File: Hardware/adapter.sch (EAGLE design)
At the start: 6 parts

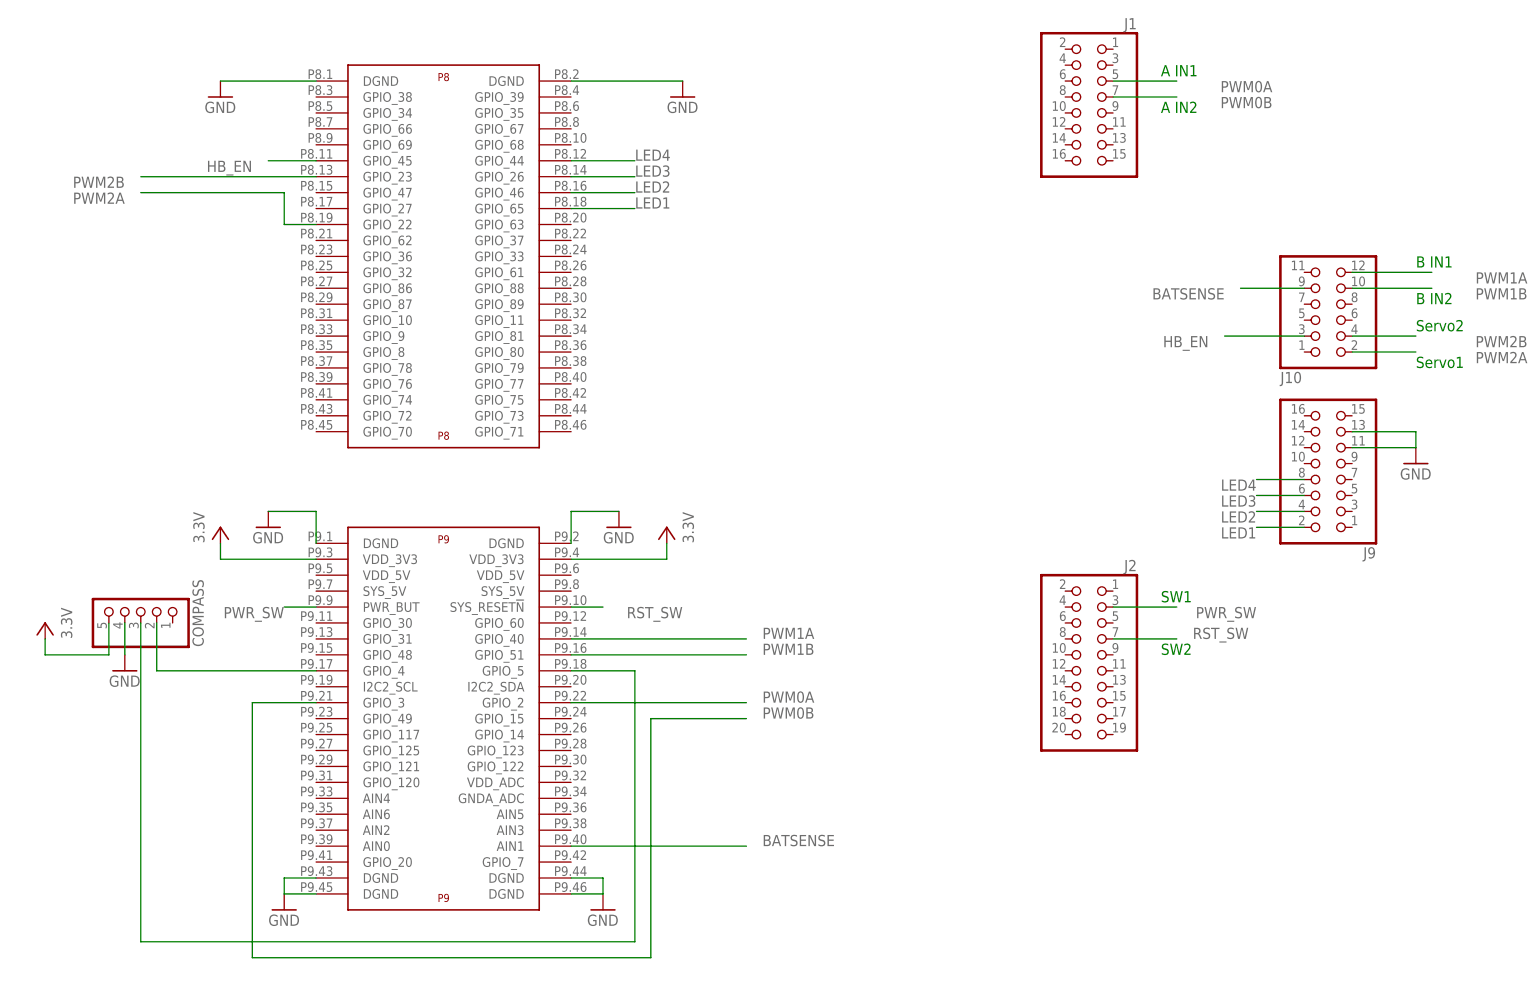
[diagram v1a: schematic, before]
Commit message: Added 5V regulator. Fixed J9 flip issue.
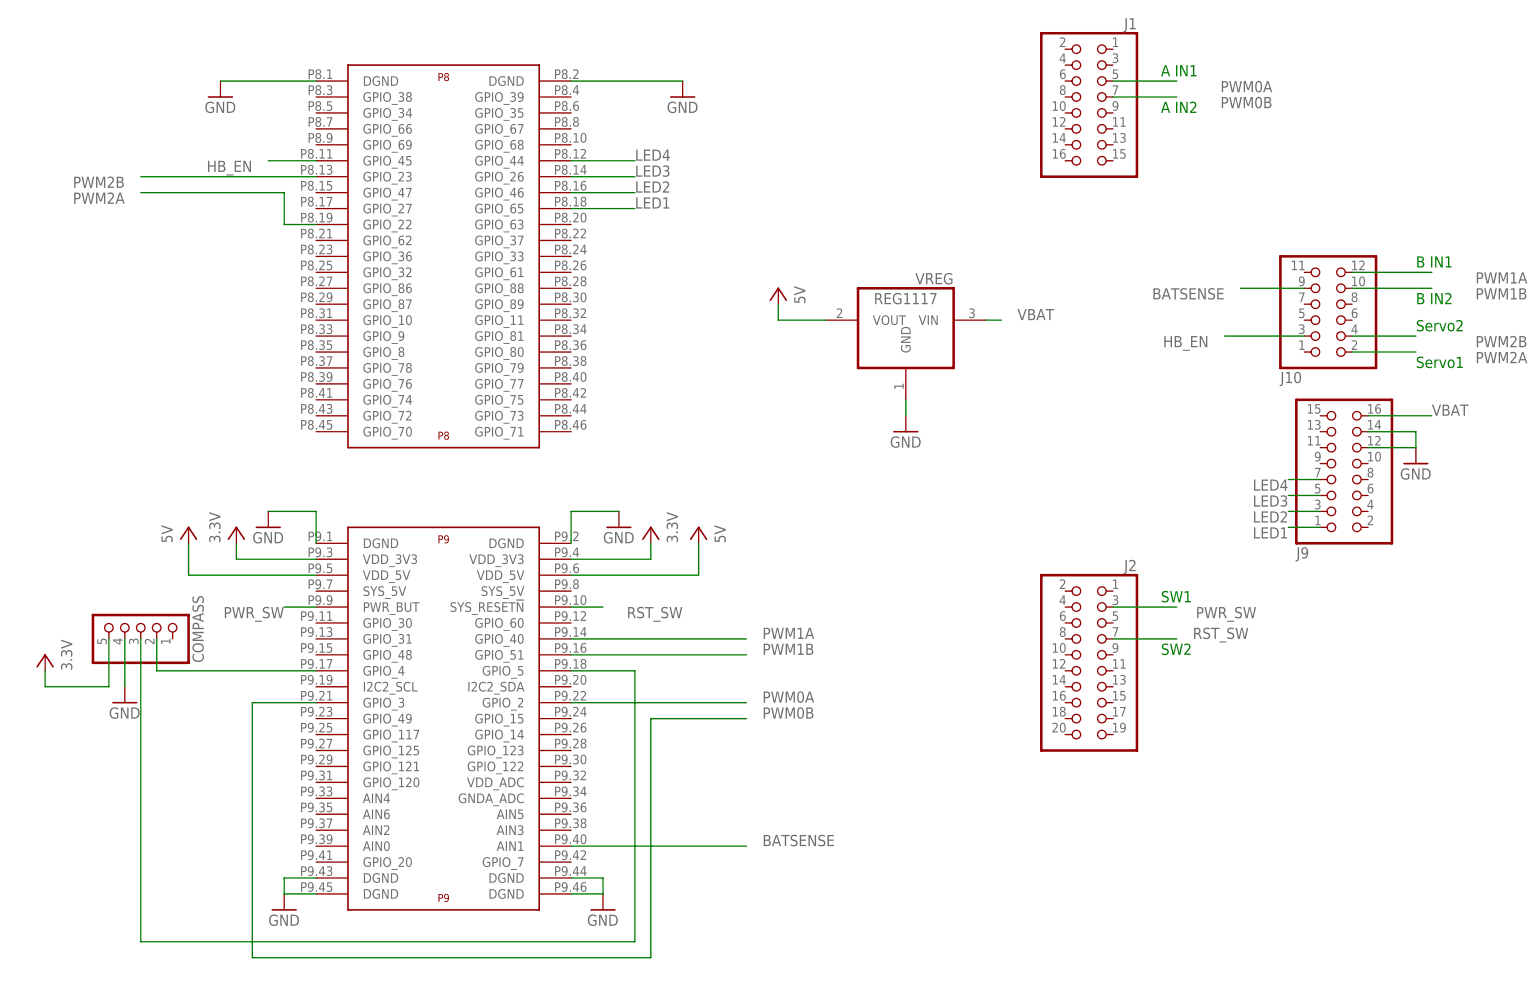
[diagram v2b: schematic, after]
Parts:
- added VREG: REG1117, burr-brown:REG1117
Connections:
- new net 5V: U$1P9.VDD_5V@1, U$1P9.VDD_5V@2, VREG.VOUT
- new net VBAT: J9.16, VREG.VIN
- net GND: now also J9.12, J9.14, VREG.GND; no longer J9.11, J9.13
- net LED1: now also J9.1; no longer J9.2
- net LED2: now also J9.3; no longer J9.4
- net LED3: now also J9.5; no longer J9.6
- net LED4: now also J9.7; no longer J9.8
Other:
- moved on the sheet: COMPASS, J9
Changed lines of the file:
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@@
 <part name="J1" library="pinhead" deviceset="PINHD-2X8" device=""/>
 <part name="J9" library="pinhead" deviceset="PINHD-2X8" device=""/>
+<part name="VREG" library="burr-brown" deviceset="REG1117" device=""/>
+<part name="GND9" library="supply1" deviceset="GND" device=""/>
+<part name="5V" library="supply1" deviceset="VCC" device="" value="5V"/>
+<part name="5V1" library="supply1" deviceset="VCC" device="" value="5V"/>
+<part name="5V2" library="supply1" deviceset="VCC" device="" value="5V"/>
 </parts>
 <sheets>
@@
 <instance part="GND6" gate="1" x="43.18" y="-10.16"/>
 <instance part="GND7" gate="1" x="172.72" y="60.96"/>
-<instance part="COMPASS" gate="A" x="-30.48" y="38.1" rot="MR90"/>
-<instance part="GND8" gate="1" x="-33.02" y="27.94"/>
-<instance part="P+1" gate="VCC" x="-45.72" y="35.56" rot="MR0"/>
-<instance part="P+2" gate="VCC" x="-17.78" y="50.8"/>
-<instance part="P+3" gate="VCC" x="53.34" y="50.8" rot="MR0"/>
+<instance part="COMPASS" gate="A" x="-30.48" y="35.56" rot="MR90"/>
+<instance part="GND8" gate="1" x="-33.02" y="22.86"/>
+<instance part="P+1" gate="VCC" x="-45.72" y="30.48" rot="MR0"/>
+<instance part="P+2" gate="VCC" x="-15.24" y="50.8"/>
+<instance part="P+3" gate="VCC" x="50.8" y="50.8" rot="MR0"/>
 <instance part="J1" gate="A" x="121.92" y="119.38" rot="MR0"/>
-<instance part="J9" gate="A" x="160.02" y="58.42" rot="R180"/>
+<instance part="J9" gate="A" x="160.02" y="58.42" rot="MR180"/>
+<instance part="VREG" gate="G$1" x="91.44" y="83.82" rot="MR0"/>
+<instance part="GND9" gate="1" x="91.44" y="66.04"/>
+<instance part="5V" gate="VCC" x="71.12" y="88.9" rot="MR0"/>
+<instance part="5V1" gate="VCC" x="58.42" y="50.8" rot="MR0"/>
+<instance part="5V2" gate="VCC" x="-22.86" y="50.8"/>
 </instances>
 <busses>
@@
 <segment>
 <pinref part="COMPASS" gate="A" pin="4"/>
-<wire x1="-33.02" y1="35.56" x2="-33.02" y2="30.48" width="0.1524" layer="91"/>
+<wire x1="-33.02" y1="33.02" x2="-33.02" y2="25.4" width="0.1524" layer="91"/>
 <pinref part="GND8" gate="1" pin="GND"/>
 </segment>
@@
 </segment>
 <segment>
+<pinref part="GND9" gate="1" pin="GND"/>
+<pinref part="VREG" gate="G$1" pin="GND"/>
+<wire x1="91.44" y1="68.58" x2="91.44" y2="71.12" width="0.1524" layer="91"/>
+</segment>
+<segment>
+<pinref part="J9" gate="A" pin="14"/>
 <pinref part="GND7" gate="1" pin="GND"/>
-<wire x1="162.56" y1="63.5" x2="172.72" y2="63.5" width="0.1524" layer="91"/>
-<wire x1="172.72" y1="63.5" x2="172.72" y2="66.04" width="0.1524" layer="91"/>
-<wire x1="172.72" y1="66.04" x2="162.56" y2="66.04" width="0.1524" layer="91"/>
-<pinref part="J9" gate="A" pin="11"/>
-<pinref part="J9" gate="A" pin="13"/>
+<wire x1="165.1" y1="66.04" x2="172.72" y2="66.04" width="0.1524" layer="91"/>
+<wire x1="172.72" y1="66.04" x2="172.72" y2="63.5" width="0.1524" layer="91"/>
+<pinref part="J9" gate="A" pin="12"/>
+<wire x1="172.72" y1="63.5" x2="165.1" y2="63.5" width="0.1524" layer="91"/>
 </segment>
 </net>
@@
 <segment>
 <pinref part="COMPASS" gate="A" pin="2"/>
-<wire x1="-27.94" y1="27.94" x2="-27.94" y2="35.56" width="0.1524" layer="91"/>
+<wire x1="-27.94" y1="27.94" x2="-27.94" y2="33.02" width="0.1524" layer="91"/>
 <pinref part="U$1" gate="P9" pin="GPIO_4"/>
 <wire x1="-27.94" y1="27.94" x2="-2.54" y2="27.94" width="0.1524" layer="91"/>
@@
 <segment>
 <pinref part="COMPASS" gate="A" pin="5"/>
-<wire x1="-35.56" y1="35.56" x2="-35.56" y2="30.48" width="0.1524" layer="91"/>
+<wire x1="-35.56" y1="33.02" x2="-35.56" y2="25.4" width="0.1524" layer="91"/>
 <pinref part="P+1" gate="VCC" pin="VCC"/>
-<wire x1="-35.56" y1="30.48" x2="-45.72" y2="30.48" width="0.1524" layer="91"/>
-<wire x1="-45.72" y1="30.48" x2="-45.72" y2="33.02" width="0.1524" layer="91"/>
+<wire x1="-35.56" y1="25.4" x2="-45.72" y2="25.4" width="0.1524" layer="91"/>
+<wire x1="-45.72" y1="25.4" x2="-45.72" y2="27.94" width="0.1524" layer="91"/>
 </segment>
 <segment>
 <pinref part="P+2" gate="VCC" pin="VCC"/>
-<wire x1="-17.78" y1="48.26" x2="-17.78" y2="45.72" width="0.1524" layer="91"/>
+<wire x1="-15.24" y1="48.26" x2="-15.24" y2="45.72" width="0.1524" layer="91"/>
 <pinref part="U$1" gate="P9" pin="VDD_3V3@1"/>
-<wire x1="-17.78" y1="45.72" x2="-2.54" y2="45.72" width="0.1524" layer="91"/>
+<wire x1="-15.24" y1="45.72" x2="-2.54" y2="45.72" width="0.1524" layer="91"/>
 </segment>
 <segment>
 <pinref part="U$1" gate="P9" pin="VDD_3V3@2"/>
-<wire x1="38.1" y1="45.72" x2="53.34" y2="45.72" width="0.1524" layer="91"/>
+<wire x1="38.1" y1="45.72" x2="50.8" y2="45.72" width="0.1524" layer="91"/>
 <pinref part="P+3" gate="VCC" pin="VCC"/>
-<wire x1="53.34" y1="45.72" x2="53.34" y2="48.26" width="0.1524" layer="91"/>
+<wire x1="50.8" y1="45.72" x2="50.8" y2="48.26" width="0.1524" layer="91"/>
 </segment>
 </net>
@@
 <segment>
 <pinref part="COMPASS" gate="A" pin="3"/>
-<wire x1="-30.48" y1="35.56" x2="-30.48" y2="-15.24" width="0.1524" layer="91"/>
+<wire x1="-30.48" y1="33.02" x2="-30.48" y2="-15.24" width="0.1524" layer="91"/>
 <wire x1="-30.48" y1="-15.24" x2="48.26" y2="-15.24" width="0.1524" layer="91"/>
 <wire x1="48.26" y1="-15.24" x2="48.26" y2="27.94" width="0.1524" layer="91"/>
@@
 <net name="LED1" class="0">
 <segment>
-<wire x1="154.94" y1="50.8" x2="147.32" y2="50.8" width="0.1524" layer="91"/>
-<pinref part="J9" gate="A" pin="2"/>
-<label x="147.32" y="50.8" size="1.778" layer="95" rot="R180"/>
-</segment>
-<segment>
 <pinref part="U$1" gate="P8" pin="GPIO_65"/>
 <wire x1="38.1" y1="101.6" x2="48.26" y2="101.6" width="0.1524" layer="91"/>
 <label x="48.26" y="101.6" size="1.778" layer="95"/>
 </segment>
+<segment>
+<pinref part="J9" gate="A" pin="1"/>
+<wire x1="157.48" y1="50.8" x2="152.4" y2="50.8" width="0.1524" layer="91"/>
+<label x="152.4" y="50.8" size="1.778" layer="95" rot="R180"/>
+</segment>
 </net>
 <net name="LED2" class="0">
-<segment>
-<wire x1="154.94" y1="53.34" x2="147.32" y2="53.34" width="0.1524" layer="91"/>
-<pinref part="J9" gate="A" pin="4"/>
-<label x="147.32" y="53.34" size="1.778" layer="95" rot="R180"/>
-</segment>
 <segment>
 <pinref part="U$1" gate="P8" pin="GPIO_46"/>
@@
 <label x="48.26" y="104.14" size="1.778" layer="95"/>
 </segment>
+<segment>
+<pinref part="J9" gate="A" pin="3"/>
+<wire x1="157.48" y1="53.34" x2="152.4" y2="53.34" width="0.1524" layer="91"/>
+<label x="152.4" y="53.34" size="1.778" layer="95" rot="R180"/>
+</segment>
 </net>
 <net name="LED3" class="0">
-<segment>
-<wire x1="154.94" y1="55.88" x2="147.32" y2="55.88" width="0.1524" layer="91"/>
-<pinref part="J9" gate="A" pin="6"/>
-<label x="147.32" y="55.88" size="1.778" layer="95" rot="R180"/>
-</segment>
 <segment>
 <pinref part="U$1" gate="P8" pin="GPIO_26"/>
@@
 <label x="48.26" y="106.68" size="1.778" layer="95"/>
 </segment>
+<segment>
+<pinref part="J9" gate="A" pin="5"/>
+<wire x1="157.48" y1="55.88" x2="152.4" y2="55.88" width="0.1524" layer="91"/>
+<label x="152.4" y="55.88" size="1.778" layer="95" rot="R180"/>
+</segment>
 </net>
 <net name="LED4" class="0">
-<segment>
-<wire x1="154.94" y1="58.42" x2="147.32" y2="58.42" width="0.1524" layer="91"/>
-<pinref part="J9" gate="A" pin="8"/>
-<label x="147.32" y="58.42" size="1.778" layer="95" rot="R180"/>
-</segment>
 <segment>
 <pinref part="U$1" gate="P8" pin="GPIO_44"/>
@@
 <label x="48.26" y="109.22" size="1.778" layer="95"/>
 </segment>
-</net>
+<segment>
+<pinref part="J9" gate="A" pin="7"/>
+<wire x1="157.48" y1="58.42" x2="152.4" y2="58.42" width="0.1524" layer="91"/>
+<label x="152.4" y="58.42" size="1.778" layer="95" rot="R180"/>
+</segment>
+</net>
+<net name="VBAT" class="0">
+<segment>
+<pinref part="VREG" gate="G$1" pin="VIN"/>
+<wire x1="104.14" y1="83.82" x2="106.68" y2="83.82" width="0.1524" layer="91"/>
+<label x="109.22" y="83.82" size="1.778" layer="95"/>
+</segment>
+<segment>
+<pinref part="J9" gate="A" pin="16"/>
+<wire x1="165.1" y1="68.58" x2="175.26" y2="68.58" width="0.1524" layer="91"/>
+<label x="175.26" y="68.58" size="1.778" layer="95"/>
+</segment>
+</net>
+<net name="5V" class="0">
+<segment>
+<pinref part="VREG" gate="G$1" pin="VOUT"/>
+<pinref part="5V" gate="VCC" pin="VCC"/>
+<wire x1="78.74" y1="83.82" x2="71.12" y2="83.82" width="0.1524" layer="91"/>
+<wire x1="71.12" y1="83.82" x2="71.12" y2="86.36" width="0.1524" layer="91"/>
+</segment>
+<segment>
+<pinref part="U$1" gate="P9" pin="VDD_5V@2"/>
+<wire x1="38.1" y1="43.18" x2="58.42" y2="43.18" width="0.1524" layer="91"/>
+<wire x1="58.42" y1="43.18" x2="58.42" y2="48.26" width="0.1524" layer="91"/>
+<pinref part="5V1" gate="VCC" pin="VCC"/>
+</segment>
+<segment>
+<pinref part="U$1" gate="P9" pin="VDD_5V@1"/>
+<wire x1="-2.54" y1="43.18" x2="-22.86" y2="43.18" width="0.1524" layer="91"/>
+<pinref part="5V2" gate="VCC" pin="VCC"/>
+<wire x1="-22.86" y1="43.18" x2="-22.86" y2="48.26" width="0.1524" layer="91"/>
+</segment>
+</net>

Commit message: Update schematic to be sectioned off and organized.
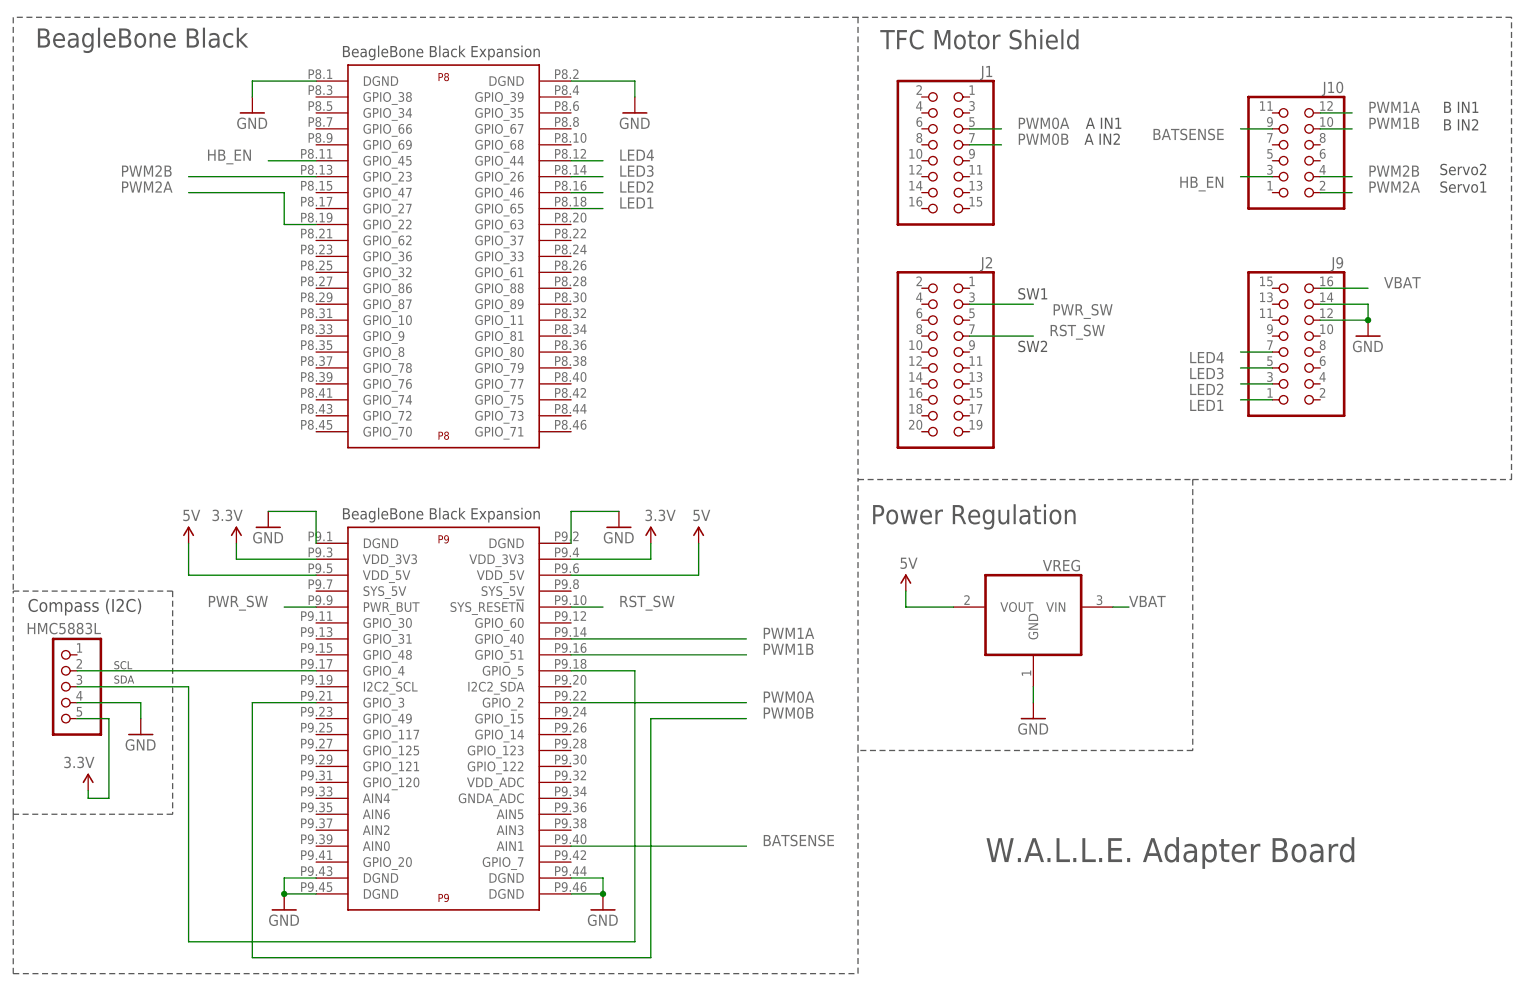
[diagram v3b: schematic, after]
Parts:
- COMPASS: value (none) -> HMC5883L
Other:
- note added: "BeagleBone Black"
- note added: "BeagleBone Black Expansion"
- note added: "Compass (I2C)"
- note added: "Power Regulation"
- note added: "SCL"
- note added: "SDA"
- note added: "TFC Motor Shield"
- note added: "W.A.L.L.E. Adapter Board"
- moved on the sheet: J1, J10, J2, J9, VREG
